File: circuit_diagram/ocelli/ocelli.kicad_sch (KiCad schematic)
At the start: 114 parts, among them J1 Conn_01x06, J2 Conn_01x06, J3 Conn_01x06, J4 Conn_01x06, J5 Conn_01x08, J6 Conn_01x02, J7 Conn_01x02, Q1 BSS138, Q10 BSS138, Q2 ST-1KL3A, Q3 TJ8S06M3L, Q4 ST-1KL3A, Q5 BSS138, Q6 ST-1KL3A, Q7 BSS138, Q8 ST-1KL3A, Q9 BSS138, SW1 SW_SPDT, SW2 TS-06104, SW3 TS-06104, SW4 TS-06104, SW5 SW_Push, SW6 SW_Push, U1 NJM2845DL1-33, U2 AS5055A, U3 AS5055A, U4 ICM-20649, U5 STM32F405RGTx, U6 DRV8835

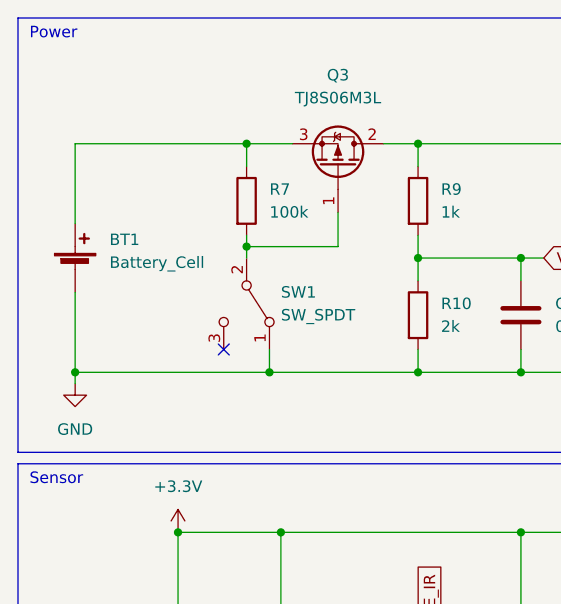
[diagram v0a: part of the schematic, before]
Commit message: バッテリー電圧の表記追加
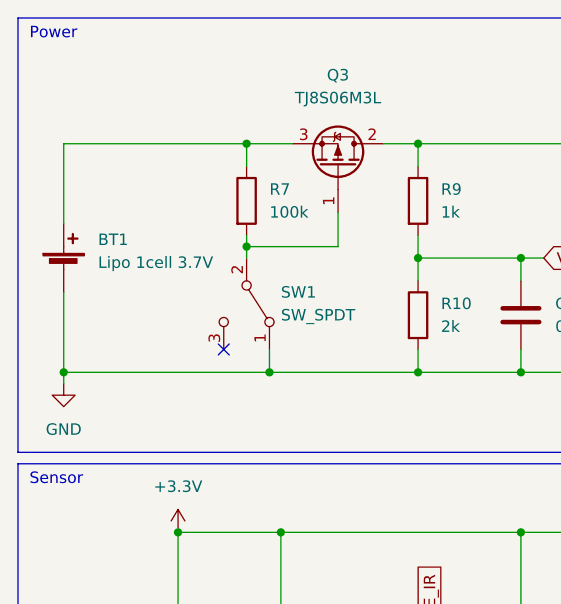
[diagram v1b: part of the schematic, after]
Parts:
- BT1: value Battery_Cell -> Lipo 1cell 3.7V
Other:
- moved on the sheet: BT1
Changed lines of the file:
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@@
   (junction (at 92.71 123.19) (diameter 0) (color 0 0 0 0)
   )
-  (junction (at 19.05 52.07) (diameter 0) (color 0 0 0 0)
+  (junction (at 17.78 52.07) (diameter 0) (color 0 0 0 0)
   )
   (junction (at 140.97 147.32) (diameter 0) (color 0 0 0 0)
@@
     (stroke (width 0) (type default) (color 0 0 0 0))
   )
-  (wire (pts (xy 19.05 26.67) (xy 38.1 26.67))
+  (wire (pts (xy 17.78 26.67) (xy 38.1 26.67))
     (stroke (width 0) (type default) (color 0 0 0 0))
   )
@@
     (stroke (width 0) (type default) (color 0 0 0 0))
   )
-  (wire (pts (xy 19.05 52.07) (xy 19.05 53.34))
+  (wire (pts (xy 17.78 52.07) (xy 17.78 53.34))
     (stroke (width 0) (type default) (color 0 0 0 0))
   )
@@
     (stroke (width 0) (type default) (color 0 0 0 0))
   )
-  (wire (pts (xy 19.05 26.67) (xy 19.05 35.56))
+  (wire (pts (xy 17.78 26.67) (xy 17.78 35.56))
     (stroke (width 0) (type default) (color 0 0 0 0))
   )
@@
     (stroke (width 0) (type default) (color 0 0 0 0))
   )
-  (wire (pts (xy 19.05 43.18) (xy 19.05 52.07))
+  (wire (pts (xy 17.78 43.18) (xy 17.78 52.07))
     (stroke (width 0) (type default) (color 0 0 0 0))
   )
@@
     (stroke (width 0) (type default) (color 0 0 0 0))
   )
-  (wire (pts (xy 40.64 52.07) (xy 19.05 52.07))
+  (wire (pts (xy 40.64 52.07) (xy 17.78 52.07))
     (stroke (width 0) (type default) (color 0 0 0 0))
   )
@@
     (pin "2")
   )
-  (symbol (lib_id "power:GND") (at 19.05 53.34 0) (unit 1)
+  (symbol (lib_id "power:GND") (at 17.78 53.34 0) (unit 1)
     (in_bom yes) (on_board yes) (fields_autoplaced)
-    (property "Reference" "#PWR0143" (id 0) (at 19.05 59.69 0)
+    (property "Reference" "#PWR0143" (id 0) (at 17.78 59.69 0)
       (effects (font (size 1.27 1.27)) hide)
     )
-    (property "Value" "GND" (id 1) (at 19.05 58.42 0))
-    (property "Footprint" "" (id 2) (at 19.05 53.34 0)
+    (property "Value" "GND" (id 1) (at 17.78 58.42 0))
+    (property "Footprint" "" (id 2) (at 17.78 53.34 0)
       (effects (font (size 1.27 1.27)) hide)
     )
-    (property "Datasheet" "" (id 3) (at 19.05 53.34 0)
+    (property "Datasheet" "" (id 3) (at 17.78 53.34 0)
       (effects (font (size 1.27 1.27)) hide)
     )
@@
     (pin "1")
   )
-  (symbol (lib_id "Device:Battery_Cell") (at 19.05 40.64 0) (unit 1)
+  (symbol (lib_id "Device:Battery_Cell") (at 17.78 40.64 0) (unit 1)
     (in_bom yes) (on_board yes) (fields_autoplaced)
-    (property "Reference" "BT1" (id 0) (at 22.86 37.3379 0)
+    (property "Reference" "BT1" (id 0) (at 21.59 37.3379 0)
       (effects (font (size 1.27 1.27)) (justify left))
     )
-    (property "Value" "Battery_Cell" (id 1) (at 22.86 39.8779 0)
+    (property "Value" "Lipo 1cell 3.7V" (id 1) (at 21.59 39.8779 0)
       (effects (font (size 1.27 1.27)) (justify left))
     )
-    (property "Footprint" "" (id 2) (at 19.05 39.116 90)
+    (property "Footprint" "" (id 2) (at 17.78 39.116 90)
       (effects (font (size 1.27 1.27)) hide)
     )
-    (property "Datasheet" "~" (id 3) (at 19.05 39.116 90)
+    (property "Datasheet" "~" (id 3) (at 17.78 39.116 90)
       (effects (font (size 1.27 1.27)) hide)
     )
@@
     )
     (path "/e3f99755-e5ce-49bf-b46f-b08d00de542b"
-      (reference "BT1") (unit 1) (value "Battery_Cell") (footprint "")
+      (reference "BT1") (unit 1) (value "Lipo 1cell 3.7V") (footprint "")
     )
     (path "/289ba81d-0fb3-4343-81df-e834a2be16f2"

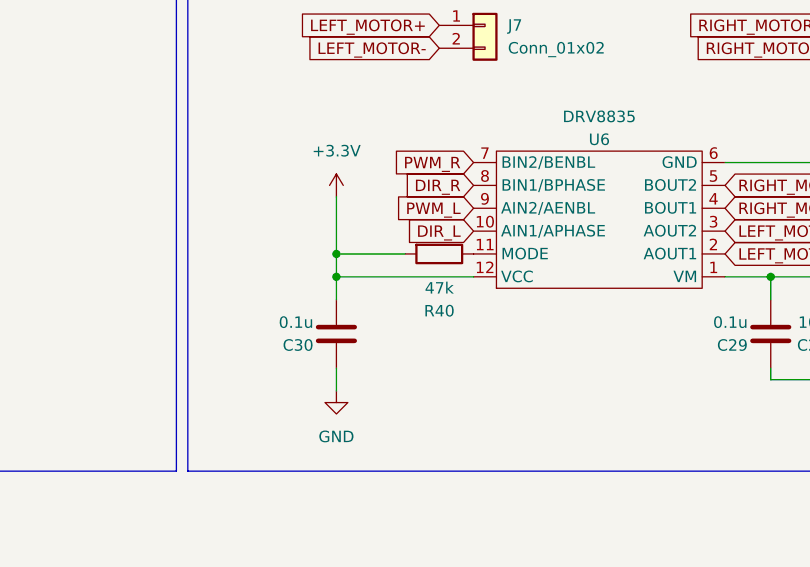
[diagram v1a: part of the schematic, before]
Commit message: モータドライバプルアップ抵抗の削除
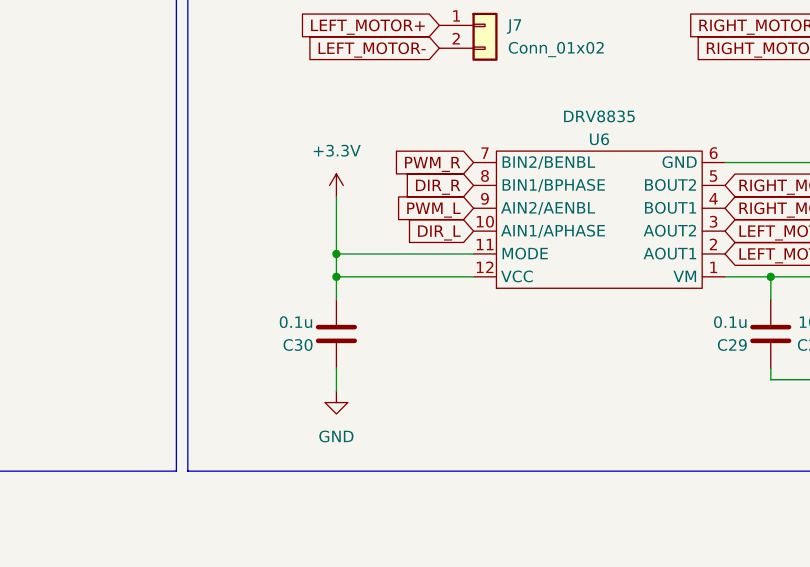
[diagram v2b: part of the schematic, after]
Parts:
- removed R40: 47k, symbol Device:R
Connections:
- net +3.3V: now also U6.11 (MODE)
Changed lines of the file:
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@@
     (stroke (width 0) (type default) (color 0 0 0 0))
   )
-  (wire (pts (xy 325.12 228.6) (xy 332.74 228.6))
+  (wire (pts (xy 325.12 228.6) (xy 340.36 228.6))
     (stroke (width 0) (type default) (color 0 0 0 0))
   )
@@
     (pin "2")
   )
-  (symbol (lib_id "Device:R") (at 336.55 228.6 270) (unit 1)
-    (in_bom yes) (on_board yes)
-    (property "Reference" "R40" (id 0) (at 336.55 234.95 90))
-    (property "Value" "47k" (id 1) (at 336.55 232.41 90))
-    (property "Footprint" "" (id 2) (at 336.55 226.822 90)
-      (effects (font (size 1.27 1.27)) hide)
-    )
-    (property "Datasheet" "~" (id 3) (at 336.55 228.6 0)
-      (effects (font (size 1.27 1.27)) hide)
-    )
-    (pin "1")
-    (pin "2")
-  )
   (symbol (lib_id "power:GND") (at 30.48 114.3 0) (unit 1)
     (in_bom yes) (on_board yes) (fields_autoplaced)
@@
       (reference "R39") (unit 1) (value "1k") (footprint "")
     )
-    (path "/b226f003-8b71-4a77-bdb3-5b25ab985d18"
-      (reference "R40") (unit 1) (value "47k") (footprint "")
-    )
     (path "/c4a6760a-1f42-4d07-8bee-e6a7174a97d8"

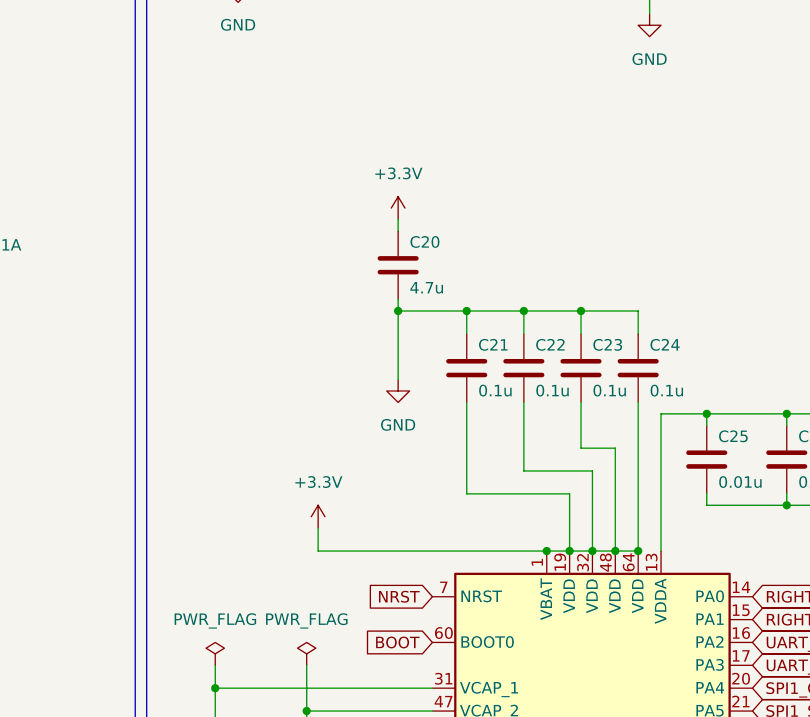
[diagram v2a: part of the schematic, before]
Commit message: マイコン電源のパスコン追加
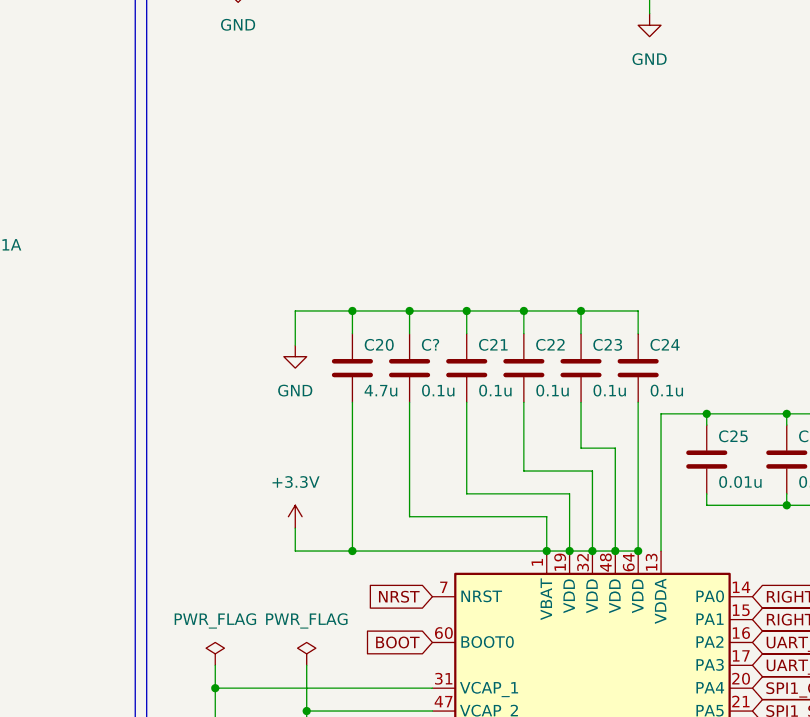
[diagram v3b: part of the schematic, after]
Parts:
- added C?: 0.1u, symbol Device:C
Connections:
- net +3.3V: now also C20.2, C?.2; no longer C20.1
- net GND: now also C20.1, C?.1; no longer C20.2
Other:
- moved on the sheet: C20
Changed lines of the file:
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@@
   (junction (at 92.71 99.06) (diameter 0) (color 0 0 0 0)
   )
+  (junction (at 224.79 127) (diameter 0) (color 0 0 0 0)
+  )
   (junction (at 142.24 52.07) (diameter 0) (color 0 0 0 0)
   )
@@
   (junction (at 127 113.03) (diameter 0) (color 0 0 0 0)
   )
+  (junction (at 224.79 100.33) (diameter 0) (color 0 0 0 0)
+  )
   (junction (at 147.32 198.12) (diameter 0) (color 0 0 0 0)
   )
@@
   (junction (at 68.58 113.03) (diameter 0) (color 0 0 0 0)
   )
-  (junction (at 229.87 100.33) (diameter 0) (color 0 0 0 0)
-  )
   (junction (at 127 161.29) (diameter 0) (color 0 0 0 0)
   )
@@
   (junction (at 41.91 113.03) (diameter 0) (color 0 0 0 0)
   )
+  (junction (at 231.14 100.33) (diameter 0) (color 0 0 0 0)
+  )
   (junction (at 120.65 26.67) (diameter 0) (color 0 0 0 0)
   )
@@
     (stroke (width 0) (type default) (color 0 0 0 0))
   )
+  (wire (pts (xy 224.79 127) (xy 246.38 127))
+    (stroke (width 0) (type default) (color 0 0 0 0))
+  )
   (wire (pts (xy 144.78 39.37) (xy 148.59 39.37))
     (stroke (width 0) (type default) (color 0 0 0 0))
@@
     (stroke (width 0) (type default) (color 0 0 0 0))
   )
-  (wire (pts (xy 229.87 100.33) (xy 229.87 107.95))
+  (wire (pts (xy 218.44 100.33) (xy 218.44 104.14))
     (stroke (width 0) (type default) (color 0 0 0 0))
   )
@@
     (stroke (width 0) (type default) (color 0 0 0 0))
   )
+  (wire (pts (xy 224.79 100.33) (xy 231.14 100.33))
+    (stroke (width 0) (type default) (color 0 0 0 0))
+  )
   (wire (pts (xy 209.55 139.7) (xy 209.55 142.24))
     (stroke (width 0) (type default) (color 0 0 0 0))
@@
     (stroke (width 0) (type default) (color 0 0 0 0))
   )
+  (wire (pts (xy 231.14 100.33) (xy 237.49 100.33))
+    (stroke (width 0) (type default) (color 0 0 0 0))
+  )
   (wire (pts (xy 88.9 254) (xy 113.03 254))
     (stroke (width 0) (type default) (color 0 0 0 0))
@@
     (stroke (width 0) (type default) (color 0 0 0 0))
   )
-  (wire (pts (xy 229.87 100.33) (xy 237.49 100.33))
+  (wire (pts (xy 218.44 100.33) (xy 224.79 100.33))
     (stroke (width 0) (type default) (color 0 0 0 0))
   )
@@
     (stroke (width 0) (type default) (color 0 0 0 0))
   )
+  (wire (pts (xy 246.38 123.19) (xy 246.38 127))
+    (stroke (width 0) (type default) (color 0 0 0 0))
+  )
   (wire (pts (xy 182.88 24.13) (xy 162.56 24.13))
     (stroke (width 0) (type default) (color 0 0 0 0))
@@
     (stroke (width 0) (type default) (color 0 0 0 0))
   )
-  (wire (pts (xy 220.98 127) (xy 246.38 127))
+  (wire (pts (xy 218.44 127) (xy 224.79 127))
     (stroke (width 0) (type default) (color 0 0 0 0))
   )
@@
     (stroke (width 0) (type default) (color 0 0 0 0))
   )
+  (wire (pts (xy 231.14 110.49) (xy 231.14 123.19))
+    (stroke (width 0) (type default) (color 0 0 0 0))
+  )
   (wire (pts (xy 163.83 243.84) (xy 163.83 246.38))
     (stroke (width 0) (type default) (color 0 0 0 0))
@@
     (stroke (width 0) (type default) (color 0 0 0 0))
   )
+  (wire (pts (xy 224.79 100.33) (xy 224.79 102.87))
+    (stroke (width 0) (type default) (color 0 0 0 0))
+  )
   (wire (pts (xy 340.36 231.14) (xy 325.12 231.14))
     (stroke (width 0) (type default) (color 0 0 0 0))
@@
     (stroke (width 0) (type default) (color 0 0 0 0))
   )
+  (wire (pts (xy 231.14 123.19) (xy 246.38 123.19))
+    (stroke (width 0) (type default) (color 0 0 0 0))
+  )
   (wire (pts (xy 85.09 43.18) (xy 85.09 52.07))
     (stroke (width 0) (type default) (color 0 0 0 0))
@@
     (stroke (width 0) (type default) (color 0 0 0 0))
   )
-  (wire (pts (xy 220.98 124.46) (xy 220.98 127))
+  (wire (pts (xy 218.44 124.46) (xy 218.44 127))
     (stroke (width 0) (type default) (color 0 0 0 0))
   )
@@
     (stroke (width 0) (type default) (color 0 0 0 0))
   )
+  (wire (pts (xy 231.14 100.33) (xy 231.14 102.87))
+    (stroke (width 0) (type default) (color 0 0 0 0))
+  )
   (wire (pts (xy 48.26 38.1) (xy 38.1 38.1))
     (stroke (width 0) (type default) (color 0 0 0 0))
@@
     (stroke (width 0) (type default) (color 0 0 0 0))
   )
+  (wire (pts (xy 224.79 110.49) (xy 224.79 127))
+    (stroke (width 0) (type default) (color 0 0 0 0))
+  )
   (wire (pts (xy 41.91 113.03) (xy 58.42 113.03))
     (stroke (width 0) (type default) (color 0 0 0 0))
@@
     (stroke (width 0) (type default) (color 0 0 0 0))
   )
-  (wire (pts (xy 229.87 99.06) (xy 229.87 100.33))
-    (stroke (width 0) (type default) (color 0 0 0 0))
-  )
   (wire (pts (xy 175.26 161.29) (xy 161.29 161.29))
     (stroke (width 0) (type default) (color 0 0 0 0))
@@
     (stroke (width 0) (type default) (color 0 0 0 0))
   )
-  (wire (pts (xy 229.87 90.17) (xy 229.87 91.44))
-    (stroke (width 0) (type default) (color 0 0 0 0))
-  )
   (wire (pts (xy 280.67 44.45) (xy 283.21 44.45))
     (stroke (width 0) (type default) (color 0 0 0 0))
@@
     (pin "2")
   )
-  (symbol (lib_id "power:+3.3V") (at 220.98 124.46 0) (unit 1)
+  (symbol (lib_id "power:+3.3V") (at 218.44 124.46 0) (unit 1)
     (in_bom yes) (on_board yes) (fields_autoplaced)
-    (property "Reference" "#PWR0109" (id 0) (at 220.98 128.27 0)
+    (property "Reference" "#PWR0109" (id 0) (at 218.44 128.27 0)
       (effects (font (size 1.27 1.27)) hide)
     )
-    (property "Value" "+3.3V" (id 1) (at 220.98 119.38 0))
-    (property "Footprint" "" (id 2) (at 220.98 124.46 0)
+    (property "Value" "+3.3V" (id 1) (at 218.44 119.38 0))
+    (property "Footprint" "" (id 2) (at 218.44 124.46 0)
       (effects (font (size 1.27 1.27)) hide)
     )
-    (property "Datasheet" "" (id 3) (at 220.98 124.46 0)
+    (property "Datasheet" "" (id 3) (at 218.44 124.46 0)
       (effects (font (size 1.27 1.27)) hide)
     )
@@
     (pin "2")
   )
-  (symbol (lib_id "power:+3.3V") (at 229.87 90.17 0) (unit 1)
-    (in_bom yes) (on_board yes) (fields_autoplaced)
-    (property "Reference" "#PWR0105" (id 0) (at 229.87 93.98 0)
-      (effects (font (size 1.27 1.27)) hide)
-    )
-    (property "Value" "+3.3V" (id 1) (at 229.87 85.09 0))
-    (property "Footprint" "" (id 2) (at 229.87 90.17 0)
-      (effects (font (size 1.27 1.27)) hide)
-    )
-    (property "Datasheet" "" (id 3) (at 229.87 90.17 0)
-      (effects (font (size 1.27 1.27)) hide)
-    )
-    (pin "1")
-  )
   (symbol (lib_id "Device:Q_Photo_NPN") (at 55.88 137.16 0) (unit 1)
     (in_bom yes) (on_board yes) (fields_autoplaced)
@@
     (pin "6")
   )
+  (symbol (lib_id "Device:C") (at 231.14 106.68 0) (unit 1)
+    (in_bom yes) (on_board yes)
+    (property "Reference" "C?" (id 0) (at 232.41 104.14 0)
+      (effects (font (size 1.27 1.27)) (justify left))
+    )
+    (property "Value" "0.1u" (id 1) (at 232.41 109.22 0)
+      (effects (font (size 1.27 1.27)) (justify left))
+    )
+    (property "Footprint" "" (id 2) (at 232.1052 110.49 0)
+      (effects (font (size 1.27 1.27)) hide)
+    )
+    (property "Datasheet" "~" (id 3) (at 231.14 106.68 0)
+      (effects (font (size 1.27 1.27)) hide)
+    )
+    (pin "1")
+    (pin "2")
+  )
   (symbol (lib_id "Device:C") (at 219.71 149.86 0) (unit 1)
     (in_bom yes) (on_board yes)
@@
     (pin "1")
   )
-  (symbol (lib_id "Device:C") (at 229.87 95.25 0) (unit 1)
+  (symbol (lib_id "Device:C") (at 224.79 106.68 0) (unit 1)
     (in_bom yes) (on_board yes)
-    (property "Reference" "C20" (id 0) (at 231.14 92.71 0)
+    (property "Reference" "C20" (id 0) (at 226.06 104.14 0)
       (effects (font (size 1.27 1.27)) (justify left))
     )
-    (property "Value" "4.7u" (id 1) (at 231.14 97.79 0)
+    (property "Value" "4.7u" (id 1) (at 226.06 109.22 0)
       (effects (font (size 1.27 1.27)) (justify left))
     )
-    (property "Footprint" "" (id 2) (at 230.8352 99.06 0)
+    (property "Footprint" "" (id 2) (at 225.7552 110.49 0)
       (effects (font (size 1.27 1.27)) hide)
     )
-    (property "Datasheet" "~" (id 3) (at 229.87 95.25 0)
+    (property "Datasheet" "~" (id 3) (at 224.79 106.68 0)
       (effects (font (size 1.27 1.27)) hide)
     )
@@
     (pin "1")
   )
-  (symbol (lib_id "power:GND") (at 229.87 107.95 0) (unit 1)
+  (symbol (lib_id "power:GND") (at 218.44 104.14 0) (unit 1)
     (in_bom yes) (on_board yes) (fields_autoplaced)
-    (property "Reference" "#PWR0110" (id 0) (at 229.87 114.3 0)
+    (property "Reference" "#PWR0110" (id 0) (at 218.44 110.49 0)
       (effects (font (size 1.27 1.27)) hide)
     )
-    (property "Value" "GND" (id 1) (at 229.87 113.03 0))
-    (property "Footprint" "" (id 2) (at 229.87 107.95 0)
+    (property "Value" "GND" (id 1) (at 218.44 109.22 0))
+    (property "Footprint" "" (id 2) (at 218.44 104.14 0)
       (effects (font (size 1.27 1.27)) hide)
     )
-    (property "Datasheet" "" (id 3) (at 229.87 107.95 0)
+    (property "Datasheet" "" (id 3) (at 218.44 104.14 0)
       (effects (font (size 1.27 1.27)) hide)
     )
@@
       (reference "#PWR0104") (unit 1) (value "GND") (footprint "")
     )
-    (path "/4b5e73bc-8f01-43ae-8e5a-7229075ee258"
-      (reference "#PWR0105") (unit 1) (value "+3.3V") (footprint "")
-    )
     (path "/17465a8c-ba0e-4776-b286-f8a07553e711"
       (reference "#PWR0106") (unit 1) (value "+BATT") (footprint "")
@@
       (reference "C30") (unit 1) (value "0.1u") (footprint "")
     )
+    (path "/5a2c25d3-64cd-481c-9a96-4ba63426ba17"
+      (reference "C?") (unit 1) (value "0.1u") (footprint "")
+    )
     (path "/04070e3e-dcba-49f1-9a5a-1fd9f7e2c5be"

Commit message: アノテーション実行
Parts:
- gave numbers to parts that had none: 1
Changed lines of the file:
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@@
   (symbol (lib_id "Device:C") (at 231.14 106.68 0) (unit 1)
     (in_bom yes) (on_board yes)
-    (property "Reference" "C?" (id 0) (at 232.41 104.14 0)
+    (property "Reference" "C31" (id 0) (at 232.41 104.14 0)
       (effects (font (size 1.27 1.27)) (justify left))
     )
@@
     )
     (path "/5a2c25d3-64cd-481c-9a96-4ba63426ba17"
-      (reference "C?") (unit 1) (value "0.1u") (footprint "")
+      (reference "C31") (unit 1) (value "0.1u") (footprint "")
     )
     (path "/04070e3e-dcba-49f1-9a5a-1fd9f7e2c5be"

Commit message: コンデンサの選定
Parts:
- C1, C10, C13, C25, C5: value 0.01u -> 0.01u 10V 5%; url (none) -> https://www.digikey.jp/ja/products/detail/murata-electronic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
- C11, C12: value 100n -> 0.1u 10V 10%; url (none) -> https://www.digikey.jp/ja/products/detail/taiyo-yuden/LMF10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
- C14, C15, C16, C18, C21, C22, C23, C24, C26, C29, C3, C30, C31, C4: value 0.1u -> 0.1u 10V 10%; url (none) -> https://www.digikey.jp/ja/products/detail/taiyo-yuden/LMF10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
- C17, C19, C9: value 2.2u -> 2.2u 6.3V 10%; url (none) -> https://www.digikey.jp/ja/products/detail/taiyo-yuden/JMK10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
- C2: value 33u -> 33u 6.3V 20%; url (none) -> https://www.digikey.jp/ja/products/detail/murata-electronic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
- C20, C7, C8: value 4.7u -> 4.7u 6.3V 10%; url (none) -> https://www.digikey.jp/ja/products/detail/taiyo-yuden/JMK10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
- C27: value 1u -> 1u 6.3V 10%; url (none) -> https://www.digikey.jp/ja/products/detail/taiyo-yuden/JMK10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
- C28: value 10u -> 10u 10V 10%; url (none) -> https://www.digikey.jp/ja/products/detail/taiyo-yuden/LMK10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
- C6: value 1u -> 1u 10V 10%; url (none) -> https://www.digikey.jp/ja/products/detail/taiyo-yuden/LMK10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
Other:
- moved on the sheet: C17, C2, C20, C21, C22, C23, C24, C26, C27, C28, C31, FB1
